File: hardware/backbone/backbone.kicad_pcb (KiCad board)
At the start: 4 copper layers, 31.3 x 68.9 mm, 80 parts, among them J1 RESET, J10 CORE_A, J11 MOUNT, J12 PW, J13 FIELD_B, J14 FIELD_A, J15 UART PROG, J16 ALED, J2 FROM_PREVIOUS, J4 FROM_PREVIOUS, J5 CONN_A, J6 BOOTLOADER, J7 CONN_B, J8 CORE_B, J9 TO NEXT, Q2 AO3401A, U11 470nH DCR=450m, U13 470nH DCR=450m, U15 ST25R100, U17 BLM18PG471SZ1D, U2 SN65HVD230DR, U4 AP2112K-3.3TRG1, U5 ESP32-C3-MINI-1-H4X, U8 G3VM-61VY3, U9 SN74AHCT1G14DCKR, X1 NX2016SA 27.12MHz

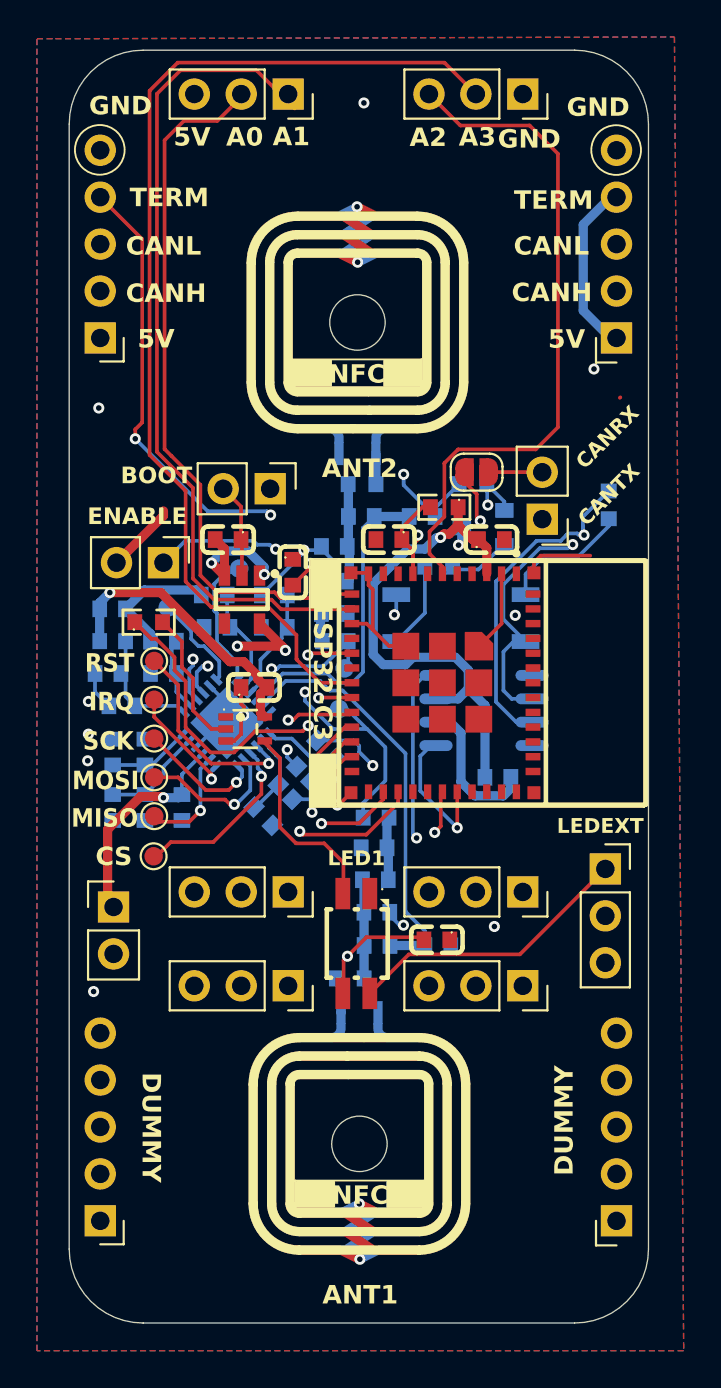
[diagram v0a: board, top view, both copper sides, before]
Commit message: fix(hardware): correct backbone antenna connectivity
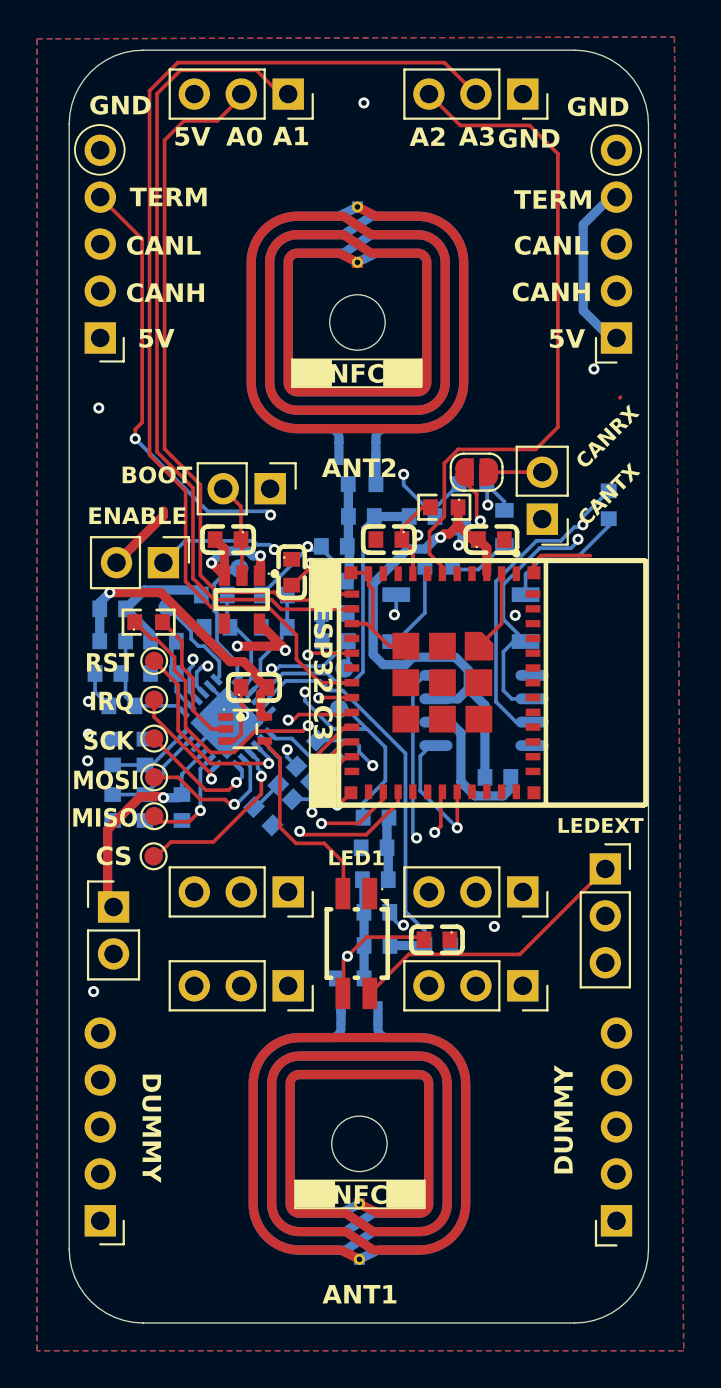
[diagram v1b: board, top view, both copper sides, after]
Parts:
- moved C9 0.06 mm to (163.8, 90.9)
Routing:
- net 5V: track 69.1 -> 83.7 mm
- net CAN_H: track 83.6 -> 82.1 mm
- net CAN_L: track 72.5 -> 73.1 mm
- net GND: track 77.6 -> 77.9 mm, vias 19 -> 17
- net Net-(ANT2-Pad2): vias 1 -> 0
- net Net-(ANT1-Pad2): vias 1 -> 0

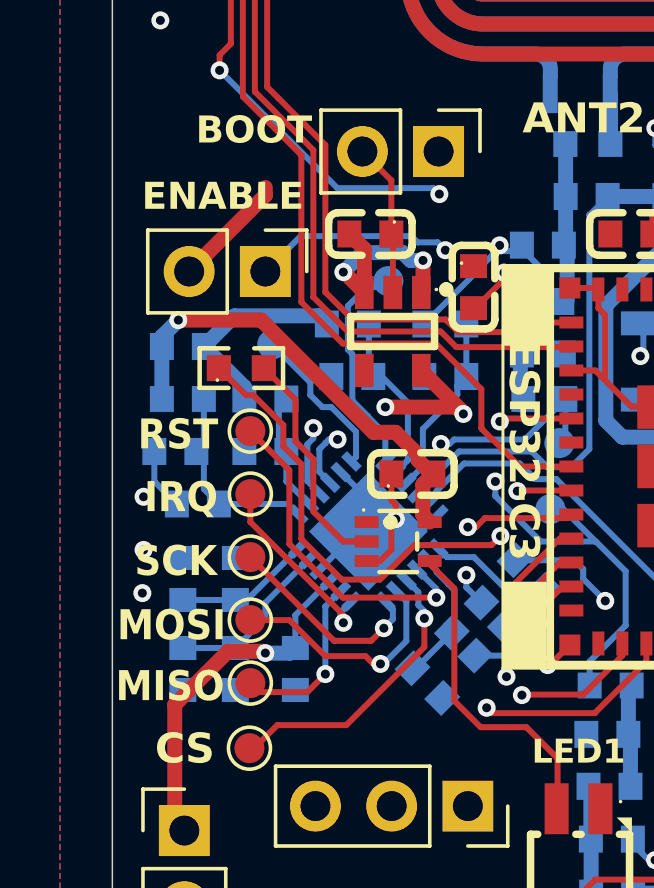
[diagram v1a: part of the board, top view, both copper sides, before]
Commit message: fix(hardware): finalize backbone routing
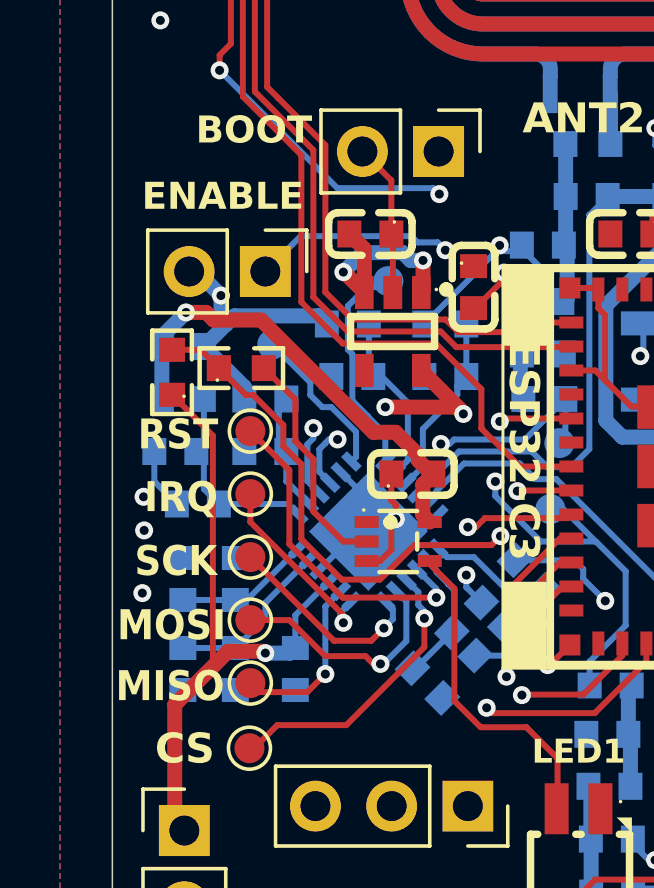
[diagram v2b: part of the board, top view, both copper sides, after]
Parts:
- added R2: 4.7k, SpaghettiLAB2:R0603, F.Cu at (153.8, 93.7)
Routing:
- net VCORE: track 75.5 -> 86.9 mm
- net LED_DATA/STRAP: track 22.5 -> 24.3 mm
- net GND: track 77.9 -> 76.5 mm, vias 17 -> 18

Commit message: chore(hardware): mark backbone revision B
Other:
- board text added: "REV B"
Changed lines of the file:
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@@
 				(font
 					(size 1.27 1.27)
+					(thickness 0.15)
 				)
 			)
@@
 				(bold yes)
 			)
+			(justify left bottom)
+		)
+	)
+	(gr_text "REV B"
+		(at 158.64 105.83 0)
+		(layer "F.SilkS" knockout)
+		(effects
+			(font
+				(size 1 1)
+				(bold yes)
+			)

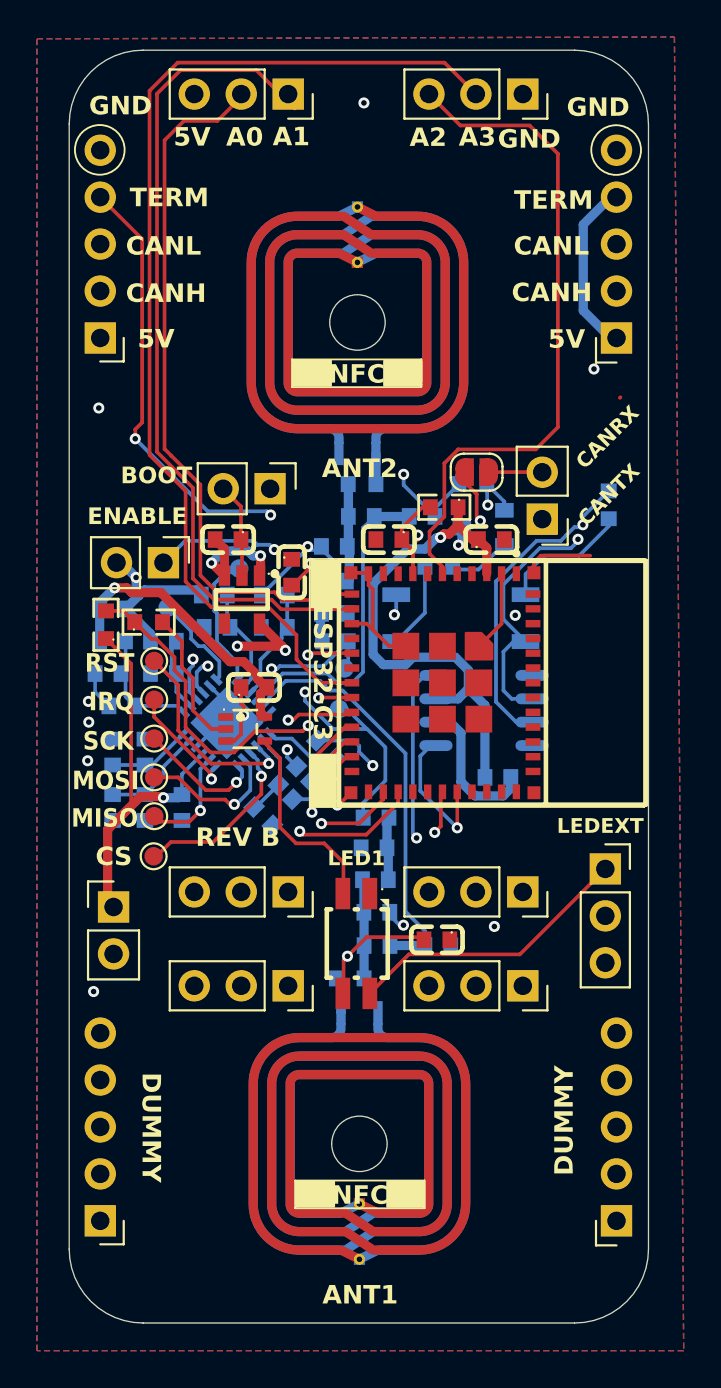
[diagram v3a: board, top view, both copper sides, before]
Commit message: Silkscreen pill style
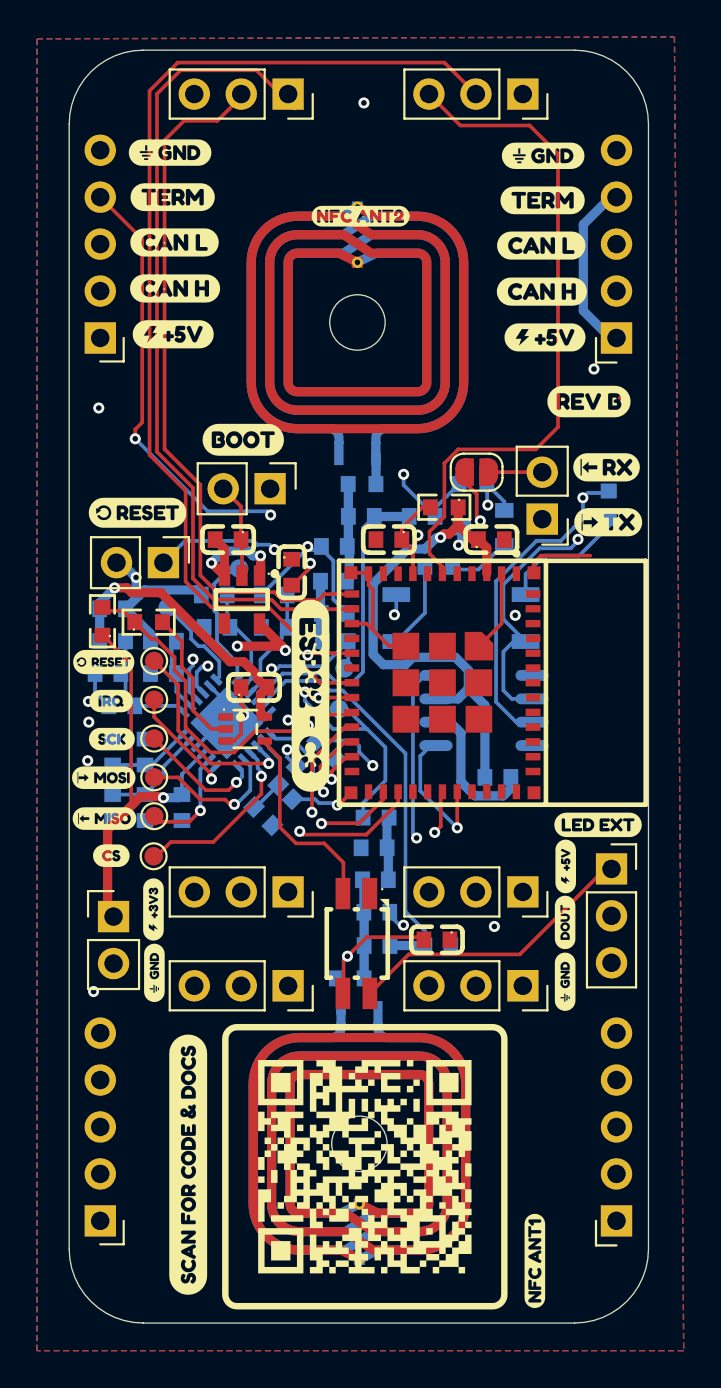
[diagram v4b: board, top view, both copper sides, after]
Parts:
- added kobee-studio-6AA825D2: Kobee Studio, kobee-studio-6AA825D2, F.Cu at (167.8, 123.1)
- added kobee-studio-6AA82C5D: Kobee Studio, kobee-studio-6AA82B88, F.Cu at (180.9, 85.2)
- added kobee-studio-6AA82C69: Kobee Studio, kobee-studio-6AA82B88, F.Cu at (181.0, 88.2)
- added kobee-studio-6AA8310F: Kobee Studio, kobee-studio-6AA82E83, F.Cu at (154.1, 97.9)
- added kobee-studio-6AA83115: Kobee Studio, kobee-studio-6AA82E83, F.Cu at (154.1, 99.9)
- added kobee-studio-6AA83128: Kobee Studio, kobee-studio-6AA82E4A, F.Cu at (154.1, 106.2)
- added kobee-studio-6AA8315A: Kobee Studio, kobee-studio-6AA82E9A, F.Cu at (153.7, 104.2)
- added kobee-studio-6AA83167: Kobee Studio, kobee-studio-6AA82EBC, F.Cu at (153.7, 102.0)
- added kobee-studio-6AA831BB: Kobee Studio, kobee-studio-6AA82ECF, F.Cu at (153.7, 95.8)
- added kobee-studio-6AA83231: Kobee Studio, kobee-studio-6AA82ECF, F.Cu at (161.2, 83.7)
- added kobee-studio-6AA83308: Kobee Studio, kobee-studio-6AA82ECF, F.Cu at (158.2, 123.0)
- added kobee-studio-6AA83490: Kobee Studio, kobee-studio-6AA82ECF, F.Cu at (179.9, 81.7)
- added kobee-studio-6AA834B7: Kobee Studio, kobee-studio-6AA82ECF, F.Cu at (180.4, 104.6)
- added kobee-studio-6AA834E9: Kobee Studio, kobee-studio-6AA834DA, F.Cu at (164.9, 97.6)
- added kobee-studio-6AA83522: Kobee Studio, kobee-studio-6AA82ECF, F.Cu at (177.0, 128.2)
- added kobee-studio-6AA83608: Kobee Studio, kobee-studio-6AA835EE, F.Cu at (177.4, 68.4)
- added kobee-studio-6AA83608: Kobee Studio, kobee-studio-6AA835EE, F.Cu at (157.3, 68.2)
- added kobee-studio-6AA836FF: Kobee Studio, kobee-studio-6AA82ECF, F.Cu at (167.6, 71.6)
- added kobee-studio-6AA83827: Kobee Studio, kobee-studio-6AA82ECF, F.Cu at (177.4, 70.8)
- added kobee-studio-6AA83827: Kobee Studio, kobee-studio-6AA82ECF, F.Cu at (157.4, 70.6)
- added kobee-studio-6AA83832: Kobee Studio, kobee-studio-6AA82ECF, F.Cu at (157.5, 73.0)
- added kobee-studio-6AA83832: Kobee Studio, kobee-studio-6AA82ECF, F.Cu at (177.3, 73.2)
- added kobee-studio-6AA83838: Kobee Studio, kobee-studio-6AA82ECF, F.Cu at (177.4, 75.7)
- added kobee-studio-6AA83838: Kobee Studio, kobee-studio-6AA82ECF, F.Cu at (157.5, 75.5)
- added kobee-studio-6AA83844: Kobee Studio, kobee-studio-6AA82ECF, F.Cu at (157.4, 78.0)
- added kobee-studio-6AA83844: Kobee Studio, kobee-studio-6AA82ECF, F.Cu at (177.6, 78.2)
- added kobee-studio-6AA83AC8: Kobee Studio, kobee-studio-6AA82ECF, F.Cu at (155.5, 87.7)
- added kobee-studio-6AA83B6C: Kobee Studio, kobee-studio-6AA835EE, F.Cu at (156.4, 112.6)
- added kobee-studio-6AA83B6C: Kobee Studio, kobee-studio-6AA835EE, F.Cu at (178.6, 113.1)
- added kobee-studio-6AA83B72: Kobee Studio, kobee-studio-6AA83B2B, F.Cu at (156.4, 109.2)
- added kobee-studio-6AA83BBD: Kobee Studio, kobee-studio-6AA83B2B, F.Cu at (178.7, 106.8)
- added kobee-studio-6AA83BE1: Kobee Studio, kobee-studio-6AA835EE, F.Cu at (178.6, 109.8)
- moved J12 0.52 mm to (154.2, 109.5)
- moved J16 0.34 mm to (181.2, 107.0)
- moved R2 0.27 mm to (153.6, 93.5)
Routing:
- net VCORE: track 86.9 -> 88.2 mm
- net CAN_H: track 82.1 -> 81.1 mm
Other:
- board text removed: "5V"
- board text removed: "A0"
- board text removed: "A1"
- board text removed: "A2"
- board text removed: "A3"
- board text removed: "BOOT"
- board text removed: "CANH"
- board text removed: "CANL"
- board text removed: "CANRX"
- board text removed: "CANTX"
- board text removed: "CS"
- board text removed: "DUMMY"
- board text removed: "ENABLE"
- board text removed: "ESP32-C3"
- board text removed: "GND"
- board text removed: "IRQ"
- board text removed: "LED1"
- board text removed: "LEDEXT"
- board text removed: "MISO"
- board text removed: "MOSI"
- board text removed: "REV B"
- board text removed: "RST"
- board text removed: "SCK"
- board text removed: "TERM"

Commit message: Fixed silkscreen text
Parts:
- removed kobee-studio-6AA83231, kobee-studio-6AA836FF: Kobee Studio, kobee-studio-6AA82ECF
- added kobee-studio-6AA93BC8: Kobee Studio, kobee-studio-6AA82ECF, F.Cu at (167.3, 80.8)
- added kobee-studio-6AA93C2C: Kobee Studio, kobee-studio-6AA82ECF, F.Cu at (161.3, 83.8)
- moved kobee-studio-6AA93B19 39.0 mm to (177.4, 120.6), turned to 90 degrees
- moved kobee-studio-6AA93B59 0.30 mm to (154.3, 106.4)
- moved kobee-studio-6AA93B49 0.12 mm to (153.7, 102.1)
- moved kobee-studio-6AA93B41 0.10 mm to (154.1, 100.0)
- turned kobee-studio-6AA93BB9 to -90 degrees
- renumbered kobee-studio-6AA83608 to kobee-studio-6AA93ACC, kobee-studio-6AA83827 to kobee-studio-6AA93AD3, kobee-studio-6AA83832 to kobee-studio-6AA93ADA, kobee-studio-6AA83838 to kobee-studio-6AA93AE3, kobee-studio-6AA83844 to kobee-studio-6AA93AEC, kobee-studio-6AA83844 to kobee-studio-6AA93AF1, kobee-studio-6AA83838 to kobee-studio-6AA93AF7, kobee-studio-6AA83832 to kobee-studio-6AA93AFD, kobee-studio-6AA83827 to kobee-studio-6AA93B02, kobee-studio-6AA83608 to kobee-studio-6AA93B08, kobee-studio-6AA83490 to kobee-studio-6AA93B19, kobee-studio-6AA82C5D to kobee-studio-6AA93B20, kobee-studio-6AA82C69 to kobee-studio-6AA93B26, kobee-studio-6AA831BB to kobee-studio-6AA93B33, kobee-studio-6AA8310F to kobee-studio-6AA93B3B, kobee-studio-6AA83115 to kobee-studio-6AA93B41, kobee-studio-6AA83167 to kobee-studio-6AA93B49, kobee-studio-6AA8315A to kobee-studio-6AA93B50, kobee-studio-6AA83128 to kobee-studio-6AA93B59, kobee-studio-6AA834B7 to kobee-studio-6AA93B92, kobee-studio-6AA83522 to kobee-studio-6AA93BB9
